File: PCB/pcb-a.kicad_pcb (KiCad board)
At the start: 2 copper layers, 116.3 x 50.4 mm, 31 parts, among them Q3 BC337, Q4 BC337, SW1 config, U1 MCP23008-xP, U4 ATmega16L-8P

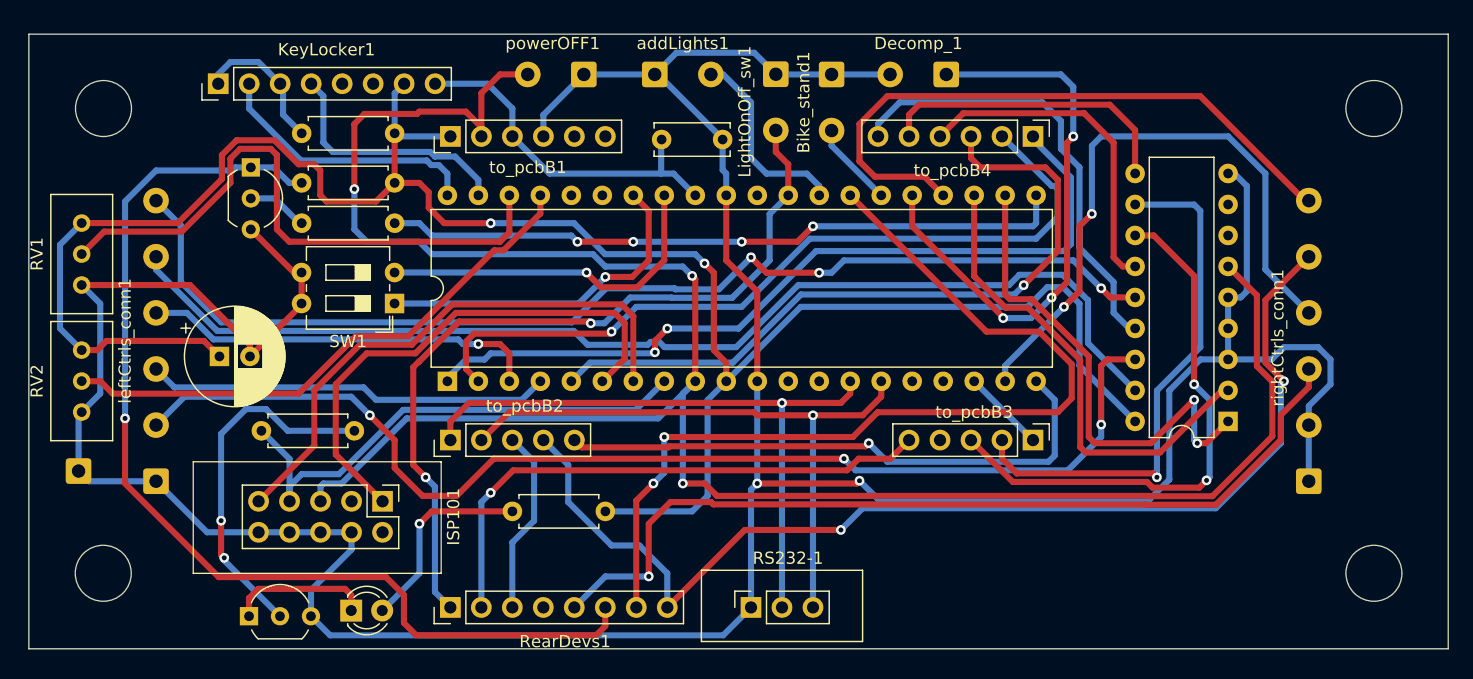
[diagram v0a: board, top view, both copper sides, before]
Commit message: Fix for (USB-ASP compliant) ISP-10pin connector
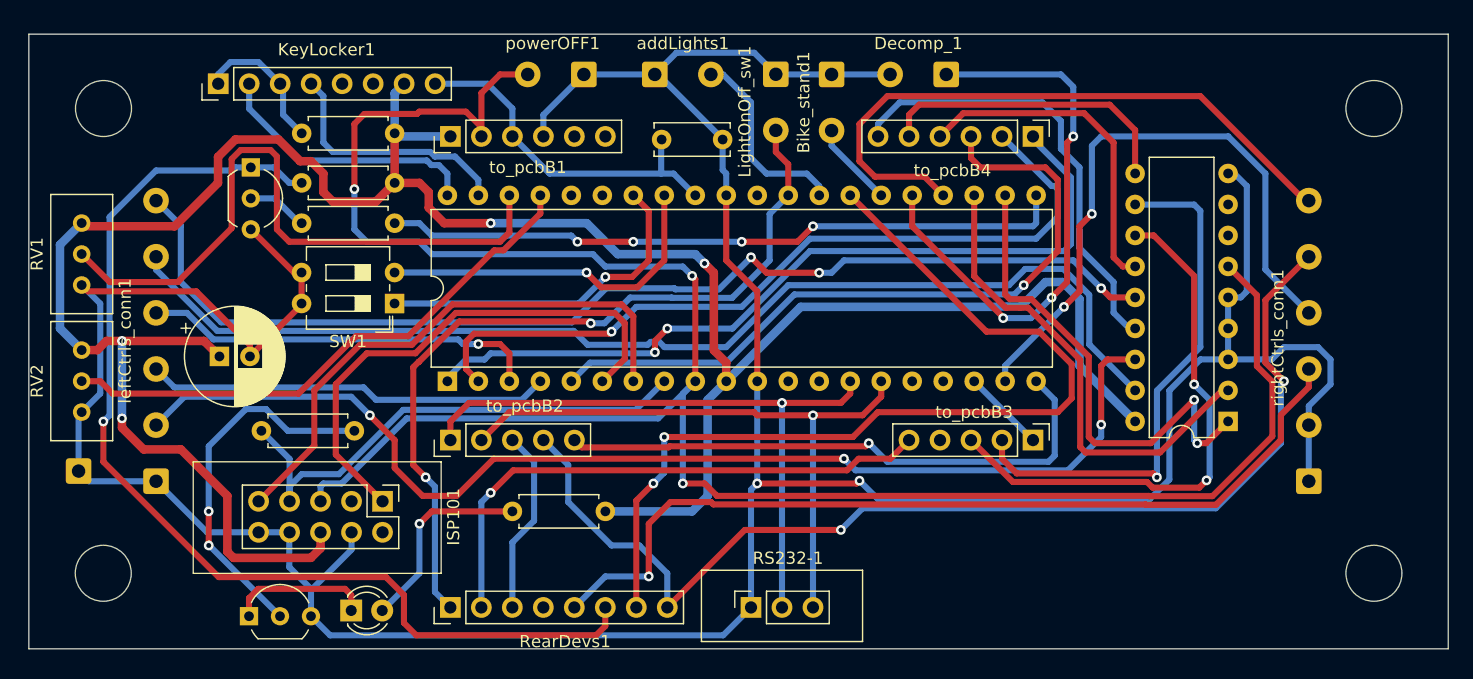
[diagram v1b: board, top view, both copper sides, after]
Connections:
- ISP101 pad 6: GND -> tempPower
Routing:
- net tempPower: track 173.1 -> 205.9 mm, vias 2 -> 4
- net Net-(RV1-Pad2): track 49.9 -> 53.8 mm
- net c_startEngine: track 87.0 -> 88.5 mm
- net Net-(Q4-Pad2): track 29.4 -> 30.3 mm
- net i_rightArrow: track 92.6 -> 93.3 mm

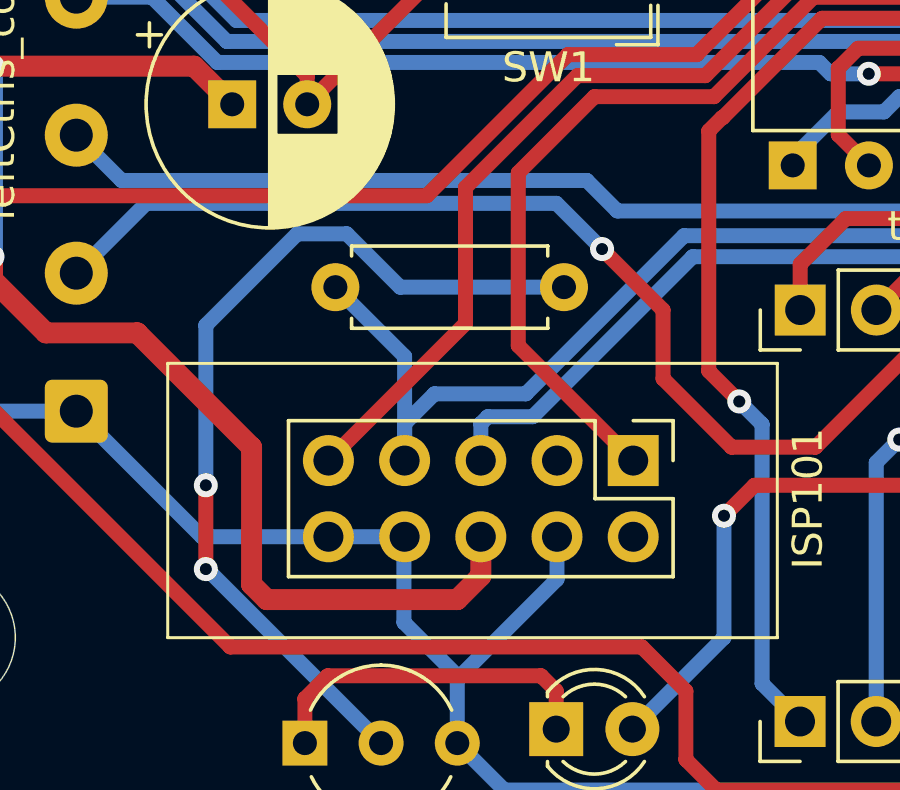
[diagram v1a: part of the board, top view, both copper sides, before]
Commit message: Wrong position for VTAG pin fixed
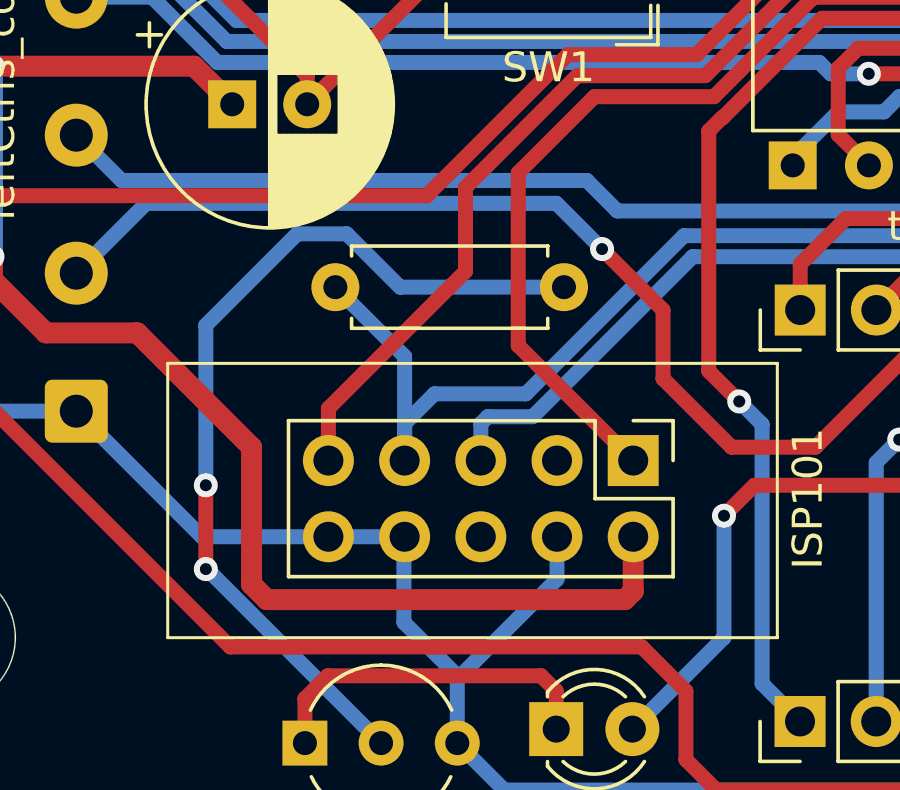
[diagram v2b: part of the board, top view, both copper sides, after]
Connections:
- ISP101 pad 2: unconnected-(ISP101-Pad2) -> tempPower
- ISP101 pad 6: tempPower -> unconnected-(ISP101-Pad6)
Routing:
- net tempPower: track 205.9 -> 211.3 mm
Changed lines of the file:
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@@
   (net 22 "o_engineReady")
   (net 23 "o_horn")
-  (net 24 "unconnected-(ISP101-Pad2)")
+  (net 24 "unconnected-(ISP101-Pad6)")
   (net 25 "unconnected-(ISP101-Pad3)")
   (net 26 "unconnected-(to_pcbB1-Pad5)")
@@
       (net 7 "Net-(ISP101-Pad1)") (pinfunction "Pin_1") (pintype "passive"))
     (pad "2" thru_hole oval (at 2.54 0 270) (size 1.7 1.7) (drill 1) (layers *.Cu *.Mask)
-      (net 24 "unconnected-(ISP101-Pad2)") (pinfunction "Pin_2") (pintype "passive+no_connect"))
+      (net 1 "tempPower") (pinfunction "Pin_2") (pintype "passive"))
     (pad "3" thru_hole oval (at 0 2.54 270) (size 1.7 1.7) (drill 1) (layers *.Cu *.Mask)
       (net 25 "unconnected-(ISP101-Pad3)") (pinfunction "Pin_3") (pintype "passive+no_connect"))
@@
       (net 48 "i_powerOFF") (pinfunction "Pin_5") (pintype "passive"))
     (pad "6" thru_hole oval (at 2.54 5.08 270) (size 1.7 1.7) (drill 1) (layers *.Cu *.Mask)
-      (net 1 "tempPower") (pinfunction "Pin_6") (pintype "passive"))
+      (net 24 "unconnected-(ISP101-Pad6)") (pinfunction "Pin_6") (pintype "passive"))
     (pad "7" thru_hole oval (at 0 7.62 270) (size 1.7 1.7) (drill 1) (layers *.Cu *.Mask)
       (net 9 "Net-(ISP101-Pad7)") (pinfunction "Pin_7") (pintype "passive"))
@@
     (style (thickness 0.1) (arrow_length 1.27) (text_position_mode 0) (extension_height 0.58642) (extension_offset 0.5) keep_text_aligned)
   )
-  (segment (start 115.832 98.44) (end 116.34 98.948) (width 0.7) (layer "F.Cu") (net 1))
   (segment (start 129.548 68.214) (end 131.58 68.214) (width 0.7) (layer "F.Cu") (net 1))
-  (segment (start 123.474 98.164) (end 123.474 96.854) (width 0.7) (layer "F.Cu") (net 1))
+  (segment (start 107.196 87.518) (end 107.196 88.28) (width 0.7) (layer "F.Cu") (net 1))
   (segment (start 155.71 81.93) (end 156.726 82.946) (width 0.7) (layer "F.Cu") (net 1))
   (segment (start 156.726 84.47) (end 156.731 84.475) (width 0.7) (layer "F.Cu") (net 1))
@@
   (segment (start 115.07 66.085026) (end 116.497026 64.658) (width 0.7) (layer "F.Cu") (net 1))
   (segment (start 121.801 66.436) (end 122.69 66.436) (width 0.7) (layer "F.Cu") (net 1))
-  (segment (start 115.832 93.868) (end 115.832 98.44) (width 0.7) (layer "F.Cu") (net 1))
   (segment (start 111.514 71.77) (end 115.07 68.214) (width 0.7) (layer "F.Cu") (net 1))
+  (segment (start 116.34 98.948) (end 128.278 98.948) (width 0.7) (layer "F.Cu") (net 1))
+  (segment (start 108.974 90.058) (end 112.022 90.058) (width 0.7) (layer "F.Cu") (net 1))
   (segment (start 128.024 69.738) (end 129.548 68.214) (width 0.7) (layer "F.Cu") (net 1))
   (segment (start 122.69 66.436) (end 123.706 67.452) (width 0.7) (layer "F.Cu") (net 1))
-  (segment (start 122.69 98.948) (end 123.474 98.164) (width 0.7) (layer "F.Cu") (net 1))
+  (segment (start 128.278 98.948) (end 128.554 98.672) (width 0.7) (layer "F.Cu") (net 1))
   (segment (start 115.187349 82.438) (end 113.917349 81.168) (width 0.7) (layer "F.Cu") (net 1))
   (segment (start 133.612 71.516) (end 137.422 71.516) (width 0.7) (layer "F.Cu") (net 1))
   (segment (start 113.917349 81.168) (end 107.196 81.168) (width 0.7) (layer "F.Cu") (net 1))
   (segment (start 124.468 69.738) (end 128.024 69.738) (width 0.7) (layer "F.Cu") (net 1))
-  (segment (start 116.34 98.948) (end 122.69 98.948) (width 0.7) (layer "F.Cu") (net 1))
   (segment (start 155.71 75.58) (end 155.71 81.93) (width 0.7) (layer "F.Cu") (net 1))
-  (segment (start 107.196 87.518) (end 107.196 88.28) (width 0.7) (layer "F.Cu") (net 1))
+  (segment (start 128.554 98.672) (end 128.554 96.854) (width 0.7) (layer "F.Cu") (net 1))
   (segment (start 129.548 64.15) (end 129.548 68.214) (width 0.7) (layer "F.Cu") (net 1))
   (segment (start 123.706 67.452) (end 123.706 68.976) (width 0.7) (layer "F.Cu") (net 1))
   (segment (start 103.894 71.506) (end 104.158 71.77) (width 0.7) (layer "F.Cu") (net 1))
   (segment (start 105.174 81.92) (end 103.894 81.92) (width 0.7) (layer "F.Cu") (net 1))
+  (segment (start 115.832 98.44) (end 116.34 98.948) (width 0.7) (layer "F.Cu") (net 1))
+  (segment (start 123.706 68.976) (end 124.468 69.738) (width 0.7) (layer "F.Cu") (net 1))
   (segment (start 112.022 90.058) (end 115.832 93.868) (width 0.7) (layer "F.Cu") (net 1))
-  (segment (start 107.196 88.28) (end 108.974 90.058) (width 0.7) (layer "F.Cu") (net 1))
-  (segment (start 123.706 68.976) (end 124.468 69.738) (width 0.7) (layer "F.Cu") (net 1))
-  (segment (start 108.974 90.058) (end 112.022 90.058) (width 0.7) (layer "F.Cu") (net 1))
   (segment (start 132.342 68.976) (end 132.342 70.246) (width 0.7) (layer "F.Cu") (net 1))
   (segment (start 132.342 70.246) (end 133.612 71.516) (width 0.7) (layer "F.Cu") (net 1))
@@
   (segment (start 156.726 82.946) (end 156.726 84.47) (width 0.7) (layer "F.Cu") (net 1))
   (segment (start 104.158 71.77) (end 111.514 71.77) (width 0.7) (layer "F.Cu") (net 1))
+  (segment (start 107.196 88.28) (end 108.974 90.058) (width 0.7) (layer "F.Cu") (net 1))
   (segment (start 115.07 68.214) (end 115.07 66.085026) (width 0.7) (layer "F.Cu") (net 1))
   (segment (start 105.926 81.168) (end 105.174 81.92) (width 0.7) (layer "F.Cu") (net 1))
+  (segment (start 115.832 93.868) (end 115.832 98.44) (width 0.7) (layer "F.Cu") (net 1))
   (via (at 107.196 81.168) (size 0.8) (drill 0.4) (layers "F.Cu" "B.Cu") (net 1))
   (via (at 154.948 74.818) (size 0.8) (drill 0.4) (layers "F.Cu" "B.Cu") (net 1))
@@
   (segment (start 134.56035 78.8715) (end 147.5715 78.8715) (width 0.5) (layer "F.Cu") (net 7))
   (segment (start 148.411 82.635) (end 146.571 84.475) (width 0.5) (layer "F.Cu") (net 7))
-  (segment (start 122.964 89.744) (end 122.964 85.212) (width 0.5) (layer "F.Cu") (net 8))
+  (segment (start 134.2704 78.1715) (end 148.1415 78.1715) (width 0.5) (layer "F.Cu") (net 8))
+  (segment (start 126.692 81.484) (end 130.9579 81.484) (width 0.5) (layer "F.Cu") (net 8))
+  (segment (start 122.964 85.212) (end 126.692 81.484) (width 0.5) (layer "F.Cu") (net 8))
   (segment (start 130.9579 81.484) (end 134.2704 78.1715) (width 0.5) (layer "F.Cu") (net 8))
+  (segment (start 118.394 94.314) (end 118.394 92.576) (width 0.5) (layer "F.Cu") (net 8))
   (segment (start 148.1415 78.1715) (end 149.111 79.141) (width 0.5) (layer "F.Cu") (net 8))
-  (segment (start 118.394 94.314) (end 122.964 89.744) (width 0.5) (layer "F.Cu") (net 8))
-  (segment (start 134.2704 78.1715) (end 148.1415 78.1715) (width 0.5) (layer "F.Cu") (net 8))
-  (segment (start 122.964 85.212) (end 126.692 81.484) (width 0.5) (layer "F.Cu") (net 8))
+  (segment (start 122.964 88.006) (end 122.964 85.212) (width 0.5) (layer "F.Cu") (net 8))
+  (segment (start 118.394 92.576) (end 122.964 88.006) (width 0.5) (layer "F.Cu") (net 8))
   (segment (start 149.111 79.141) (end 149.111 84.475) (width 0.5) (layer "F.Cu") (net 8))
-  (segment (start 126.692 81.484) (end 130.9579 81.484) (width 0.5) (layer "F.Cu") (net 8))
   (segment (start 120.934 93.084) (end 121.928 92.09) (width 0.5) (layer "B.Cu") (net 9))
   (segment (start 130.248001 86.818) (end 149.308 86.818) (width 0.5) (layer "B.Cu") (net 9))

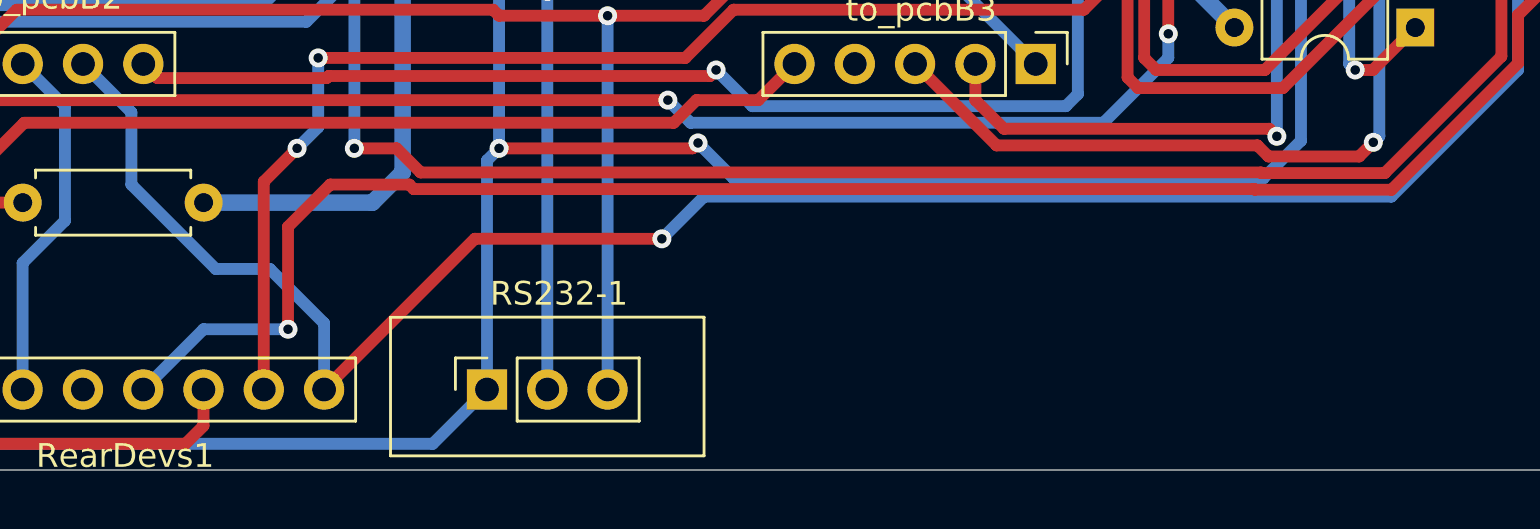
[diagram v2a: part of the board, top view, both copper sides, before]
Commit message: Fix: RESET pin and RS232 port fingerprint
- pull-up  resistor added to RESET pin
- RS232 port fingerprint resized to standard 4-pin port
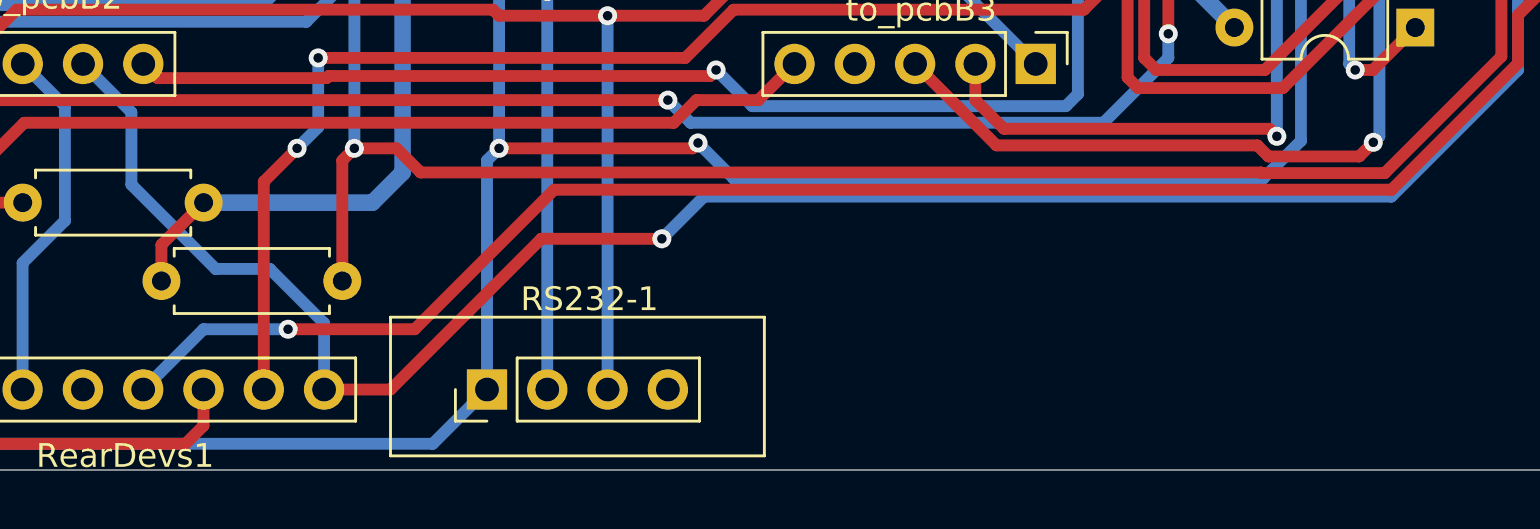
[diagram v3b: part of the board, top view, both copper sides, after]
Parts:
- added R2: 10K, Resistor_THT:R_Axial_DIN0207_L6.3mm_D2.5mm_P7.62mm_Horizontal, F.Cu at (145.0, 98.4)
- RS232-1: value RS232 -> Conn_01x04; footprint Connector_PinSocket_2.54mm:PinSocket_1x03_P2.54mm_Vertical -> Connector_PinHeader_2.54mm:PinHeader_1x04_P2.54mm_Vertical
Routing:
- net i_powerOFF: track 177.3 -> 183.1 mm
- net tempPower: track 211.3 -> 215.3 mm
- net c_brakeSwitch: track 73.1 -> 70.4 mm
